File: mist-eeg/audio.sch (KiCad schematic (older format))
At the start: 30 parts, among them J3 Audio, U10 ADAU1372, Y1 12.288 MHz @ max 20 pF

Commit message: Hooked-up the SoM
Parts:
- removed Y1: 12.288 MHz @ max 20 pF, Crystal:Crystal_SMD_Abracon_ABM8G-4Pin_3.2x2.5mm, symbol Device:Crystal_GND24_Small
- renumbered TP9 to TP10, TP5 to TP6, TP6 to TP7, TP7 to TP8, TP8 to TP9
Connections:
- net labels added: MCLK
- net labels removed: XI, XO
- wire segments 143 -> 133
- no-connect marks 2 -> 3
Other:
- note added: "TODO: protection diodes"
- note removed: "Crystal Oscillator"
- moved on the sheet: D3, R55, R56, R57, TP10, U10A

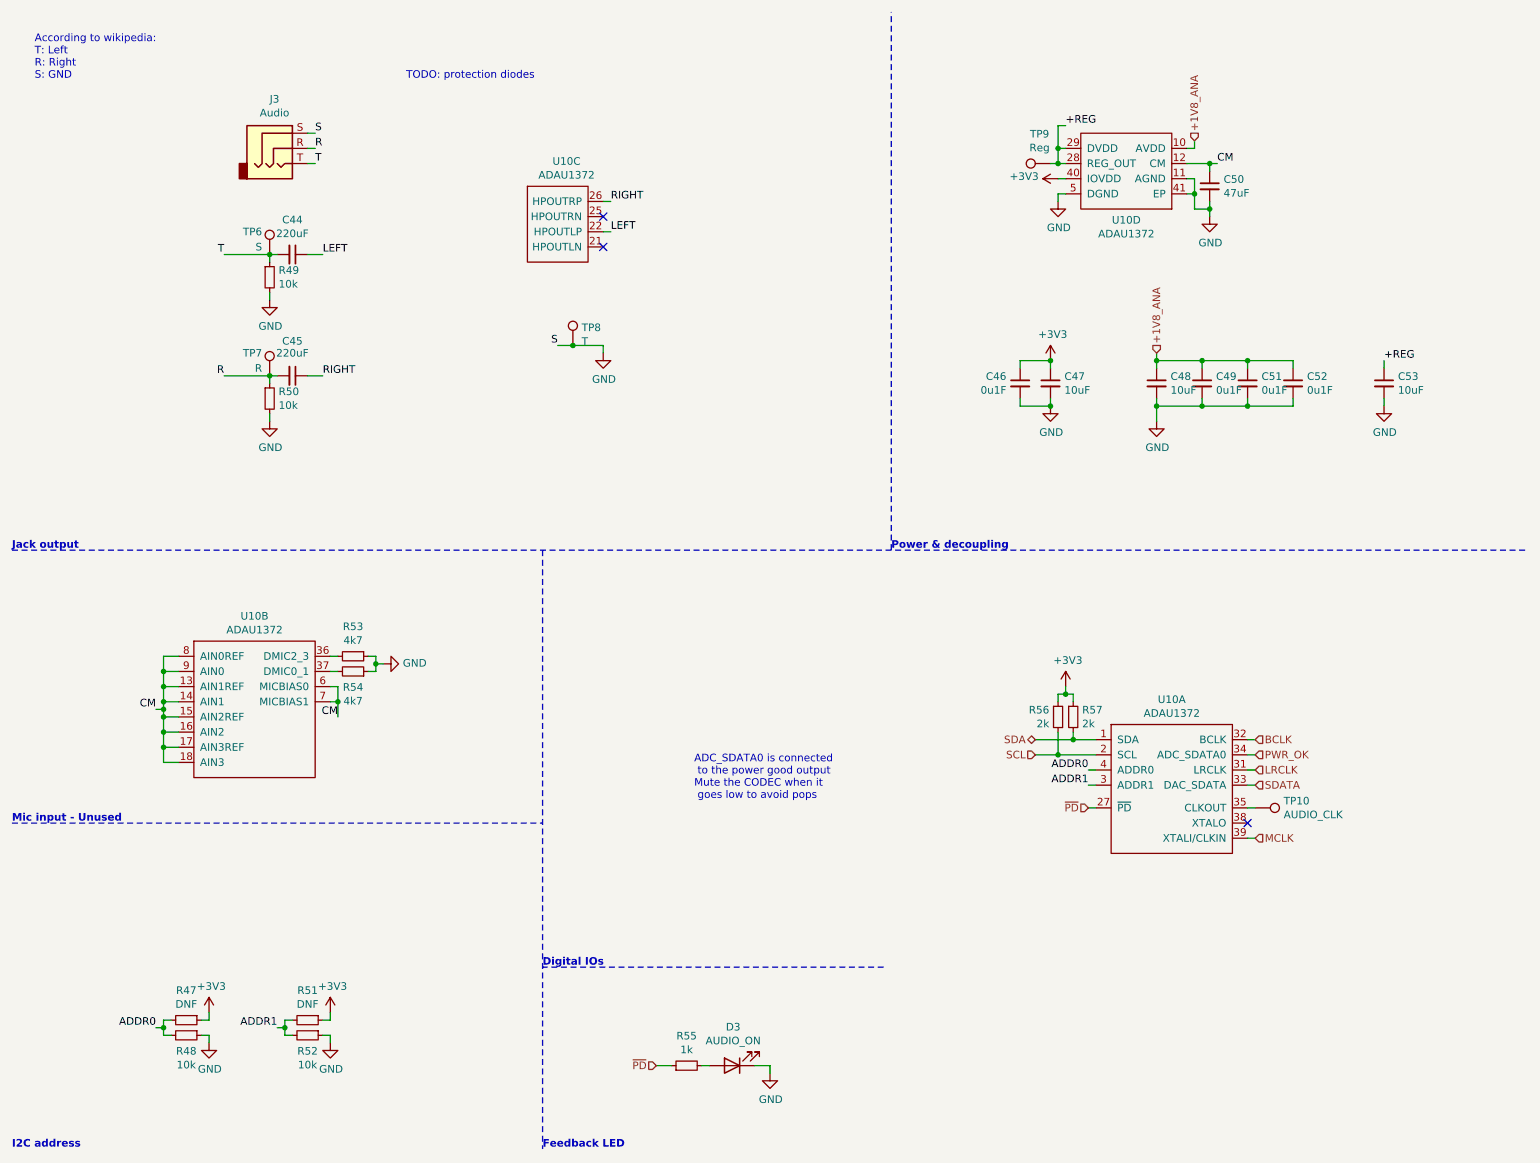
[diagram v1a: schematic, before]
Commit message: Finish schematic and create interface specifications
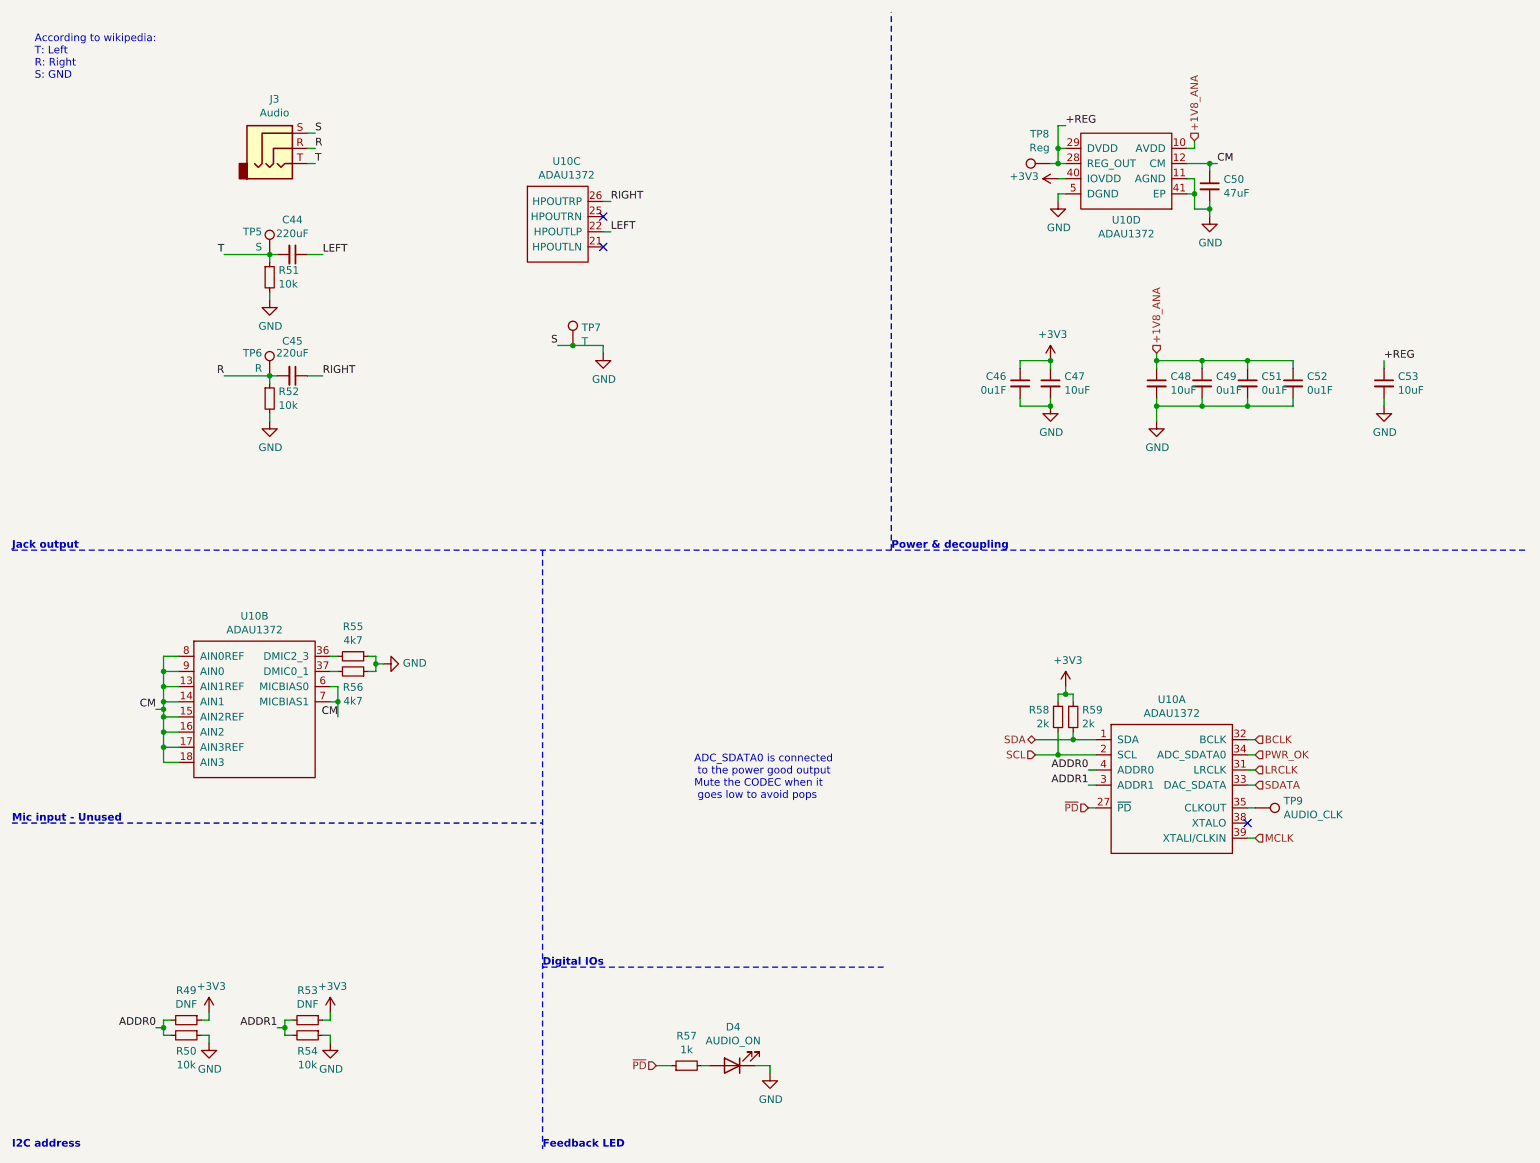
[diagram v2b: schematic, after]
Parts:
- renumbered D3 to D4, R47 to R49, R48 to R50, R49 to R51, R50 to R52, R51 to R53, R52 to R54, R53 to R55, R54 to R56, R55 to R57, R56 to R58, R57 to R59, TP6 to TP5, TP7 to TP6, TP8 to TP7, TP9 to TP8, TP10 to TP9
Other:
- note removed: "TODO: protection diodes"
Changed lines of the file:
@@
 $EndComp
 $Comp
-L Device:R_Small R49
+L Device:R_Small R51
 U 1 1 60ABF5BC
 P 2200 2250
-F 0 "R49" H 2259 2296 50  0000 L CNN
+F 0 "R51" H 2259 2296 50  0000 L CNN
 F 1 "10k" H 2259 2205 50  0000 L CNN
 F 2 "Resistor_SMD:R_0603_1608Metric" H 2200 2250 50  0001 C CNN
@@
 	2200 2400 2200 2350
 $Comp
-L Connector:TestPoint TP6
+L Connector:TestPoint TP5
 U 1 1 60AC1D50
 P 2200 2100
-F 0 "TP6" H 2150 2250 50  0000 R CNN
+F 0 "TP5" H 2150 2250 50  0000 R CNN
 F 1 "S" H 2150 2150 50  0000 R CNN
 F 2 "TestPoint:TestPoint_Pad_D1.0mm" H 2400 2100 50  0001 C CNN
@@
 $EndComp
 $Comp
-L Device:R_Small R50
+L Device:R_Small R52
 U 1 1 60AC80C7
 P 2200 3050
-F 0 "R50" H 2259 3096 50  0000 L CNN
+F 0 "R52" H 2259 3096 50  0000 L CNN
 F 1 "10k" H 2259 3005 50  0000 L CNN
 F 2 "Resistor_SMD:R_0603_1608Metric" H 2200 3050 50  0001 C CNN
@@
 	2200 3200 2200 3150
 $Comp
-L Connector:TestPoint TP8
+L Connector:TestPoint TP7
 U 1 1 60AC9A75
 P 4200 2700
-F 0 "TP8" H 4258 2818 50  0000 L CNN
+F 0 "TP7" H 4258 2818 50  0000 L CNN
 F 1 "T" H 4258 2727 50  0000 L CNN
 F 2 "TestPoint:TestPoint_Pad_D1.0mm" H 4400 2700 50  0001 C CNN
@@
 	1900 2900 2200 2900
 $Comp
-L Connector:TestPoint TP7
+L Connector:TestPoint TP6
 U 1 1 60AC80D7
 P 2200 2900
-F 0 "TP7" H 2150 3050 50  0000 R CNN
+F 0 "TP6" H 2150 3050 50  0000 R CNN
 F 1 "R" H 2150 2950 50  0000 R CNN
 F 2 "TestPoint:TestPoint_Pad_D1.0mm" H 2400 2900 50  0001 C CNN
@@
 	8300 1600 8300 1700
 $Comp
-L power:GND #PWR077
+L power:GND #PWR078
 U 1 1 60AE94E1
 P 7400 1750
-F 0 "#PWR077" H 7400 1500 50  0001 C CNN
+F 0 "#PWR078" H 7400 1500 50  0001 C CNN
 F 1 "GND" H 7405 1577 50  0000 C CNN
 F 2 "" H 7400 1750 50  0001 C CNN
@@
 	7450 1400 7400 1400
 $Comp
-L Connector:TestPoint TP9
+L Connector:TestPoint TP8
 U 1 1 60AF62E6
 P 7350 1500
-F 0 "TP9" V 7545 1572 50  0000 C CNN
+F 0 "TP8" V 7545 1572 50  0000 C CNN
 F 1 "Reg" V 7454 1572 50  0000 C CNN
 F 2 "TestPoint:TestPoint_Pad_D1.0mm" H 7550 1500 50  0001 C CNN
@@
 SCL
 $Comp
-L Device:R_Small R57
+L Device:R_Small R59
 U 1 1 60B0947B
 P 7500 5150
-F 0 "R57" H 7559 5196 50  0000 L CNN
+F 0 "R59" H 7559 5196 50  0000 L CNN
 F 1 "2k" H 7559 5105 50  0000 L CNN
 F 2 "Resistor_SMD:R_0201_0603Metric" H 7500 5150 50  0001 C CNN
@@
 	7500 5250 7500 5300
 $Comp
-L Device:R_Small R56
+L Device:R_Small R58
 U 1 1 60B0B8D0
 P 7400 5150
-F 0 "R56" H 7342 5196 50  0000 R CNN
+F 0 "R58" H 7342 5196 50  0000 R CNN
 F 1 "2k" H 7342 5105 50  0000 R CNN
 F 2 "Resistor_SMD:R_0201_0603Metric" H 7400 5150 50  0001 C CNN
@@
 ADDR0
 $Comp
-L Device:R_Small R47
+L Device:R_Small R49
 U 1 1 60B1A008
 P 1650 7150
-F 0 "R47" V 1454 7150 50  0000 C CNN
+F 0 "R49" V 1454 7150 50  0000 C CNN
 F 1 "DNF" V 1545 7150 50  0000 C CNN
 F 2 "Resistor_SMD:R_0603_1608Metric" H 1650 7150 50  0001 C CNN
@@
 	1800 7100 1800 7150
 $Comp
-L power:GND #PWR066
+L power:GND #PWR067
 U 1 1 60B1D99B
 P 1800 7300
-F 0 "#PWR066" H 1800 7050 50  0001 C CNN
+F 0 "#PWR067" H 1800 7050 50  0001 C CNN
 F 1 "GND" H 1805 7127 50  0000 C CNN
 F 2 "" H 1800 7300 50  0001 C CNN
@@
 ADDR1
 $Comp
-L Device:R_Small R51
+L Device:R_Small R53
 U 1 1 60B213C1
 P 2450 7150
-F 0 "R51" V 2254 7150 50  0000 C CNN
+F 0 "R53" V 2254 7150 50  0000 C CNN
 F 1 "DNF" V 2345 7150 50  0000 C CNN
 F 2 "Resistor_SMD:R_0603_1608Metric" H 2450 7150 50  0001 C CNN
@@
 	2600 7100 2600 7150
 $Comp
-L power:GND #PWR070
+L power:GND #PWR071
 U 1 1 60B213D6
 P 2600 7300
-F 0 "#PWR070" H 2600 7050 50  0001 C CNN
+F 0 "#PWR071" H 2600 7050 50  0001 C CNN
 F 1 "GND" H 2605 7127 50  0000 C CNN
 F 2 "" H 2600 7300 50  0001 C CNN
@@
 Power & decoupling
 $Comp
-L power:GND #PWR075
+L power:GND #PWR076
 U 1 1 60C1A59D
 P 7350 3100
-F 0 "#PWR075" H 7350 2850 50  0001 C CNN
+F 0 "#PWR076" H 7350 2850 50  0001 C CNN
 F 1 "GND" H 7355 2927 50  0000 C CNN
 F 2 "" H 7350 3100 50  0001 C CNN
@@
 	9550 2800 9550 2850
 $Comp
-L power:GND #PWR081
+L power:GND #PWR082
 U 1 1 60C65040
 P 9550 3100
-F 0 "#PWR081" H 9550 2850 50  0001 C CNN
+F 0 "#PWR082" H 9550 2850 50  0001 C CNN
 F 1 "GND" H 9555 2927 50  0000 C CNN
 F 2 "" H 9550 3100 50  0001 C CNN
@@
 	8700 5300 8650 5300
 $Comp
-L Connector:TestPoint TP10
+L Connector:TestPoint TP9
 U 1 1 60C89384
 P 8700 5750
-F 0 "TP10" V 8654 5938 50  0000 L CNN
+F 0 "TP9" V 8654 5938 50  0000 L CNN
 F 1 "AUDIO_CLK" V 8745 5938 50  0000 L CNN
 F 2 "TestPoint:TestPoint_Pad_D1.0mm" H 8900 5750 50  0001 C CNN
@@
 	8700 5750 8650 5750
 $Comp
-L Device:LED D3
+L Device:LED D4
 U 1 1 60CD54B6
 P 5250 7450
-F 0 "D3" H 5243 7195 50  0000 C CNN
+F 0 "D4" H 5243 7195 50  0000 C CNN
 F 1 "AUDIO_ON" H 5243 7286 50  0000 C CNN
 F 2 "LED_SMD:LED_0603_1608Metric" H 5250 7450 50  0001 C CNN
@@
 ~PD~
 $Comp
-L Device:R_Small R55
+L Device:R_Small R57
 U 1 1 60CD6214
 P 4950 7450
-F 0 "R55" V 5146 7450 50  0000 C CNN
+F 0 "R57" V 5146 7450 50  0000 C CNN
 F 1 "1k" V 5055 7450 50  0000 C CNN
 F 2 "Resistor_SMD:R_0402_1005Metric" H 4950 7450 50  0001 C CNN
@@
 	5050 7450 5100 7450
 $Comp
-L power:GND #PWR073
+L power:GND #PWR074
 U 1 1 60CDB6F6
 P 5500 7500
-F 0 "#PWR073" H 5500 7250 50  0001 C CNN
+F 0 "#PWR074" H 5500 7250 50  0001 C CNN
 F 1 "GND" H 5505 7327 50  0000 C CNN
 F 2 "" H 5500 7500 50  0001 C CNN
@@
 	4000 4050 4000 8000
 $Comp
-L Device:R_Small R48
+L Device:R_Small R50
 U 1 1 60B1A002
 P 1650 7250
-F 0 "R48" V 1754 7250 50  0000 C CNN
+F 0 "R50" V 1754 7250 50  0000 C CNN
 F 1 "10k" V 1845 7250 50  0000 C CNN
 F 2 "Resistor_SMD:R_0603_1608Metric" H 1650 7250 50  0001 C CNN
@@
 $EndComp
 $Comp
-L Device:R_Small R52
+L Device:R_Small R54
 U 1 1 60FB0630
 P 2450 7250
-F 0 "R52" V 2554 7250 50  0000 C CNN
+F 0 "R54" V 2554 7250 50  0000 C CNN
 F 1 "10k" V 2645 7250 50  0000 C CNN
 F 2 "Resistor_SMD:R_0603_1608Metric" H 2450 7250 50  0001 C CNN
@@
 	7400 1600 7450 1600
 $Comp
-L power:GND #PWR080
+L power:GND #PWR081
 U 1 1 611D8E7E
 P 8400 1850
-F 0 "#PWR080" H 8400 1600 50  0001 C CNN
+F 0 "#PWR081" H 8400 1600 50  0001 C CNN
 F 1 "GND" H 8405 1677 50  0000 C CNN
 F 2 "" H 8400 1850 50  0001 C CNN
@@
 $EndComp
 $Comp
-L power:GND #PWR079
+L power:GND #PWR080
 U 1 1 611D9111
 P 8050 3200
-F 0 "#PWR079" H 8050 2950 50  0001 C CNN
+F 0 "#PWR080" H 8050 2950 50  0001 C CNN
 F 1 "GND" H 8055 3027 50  0000 C CNN
 F 2 "" H 8050 3200 50  0001 C CNN
@@
 $EndComp
 $Comp
-L power:GND #PWR072
+L power:GND #PWR073
 U 1 1 611D94F5
 P 4400 2750
-F 0 "#PWR072" H 4400 2500 50  0001 C CNN
+F 0 "#PWR073" H 4400 2500 50  0001 C CNN
 F 1 "GND" H 4405 2577 50  0000 C CNN
 F 2 "" H 4400 2750 50  0001 C CNN
@@
 $EndComp
 $Comp
-L power:GND #PWR067
+L power:GND #PWR068
 U 1 1 611DC98D
 P 2200 2400
-F 0 "#PWR067" H 2200 2150 50  0001 C CNN
+F 0 "#PWR068" H 2200 2150 50  0001 C CNN
 F 1 "GND" H 2205 2227 50  0000 C CNN
 F 2 "" H 2200 2400 50  0001 C CNN
@@
 $EndComp
 $Comp
-L power:GND #PWR068
+L power:GND #PWR069
 U 1 1 611DCDAF
 P 2200 3200
-F 0 "#PWR068" H 2200 2950 50  0001 C CNN
+F 0 "#PWR069" H 2200 2950 50  0001 C CNN
 F 1 "GND" H 2205 3027 50  0000 C CNN
 F 2 "" H 2200 3200 50  0001 C CNN
@@
 	2650 4750 2600 4750
 $Comp
-L power:GND #PWR071
+L power:GND #PWR072
 U 1 1 60B73760
 P 2950 4800
-F 0 "#PWR071" H 2950 4550 50  0001 C CNN
+F 0 "#PWR072" H 2950 4550 50  0001 C CNN
 F 1 "GND" V 2955 4672 50  0000 R CNN
 F 2 "" H 2950 4800 50  0001 C CNN
@@
 	2900 4800 2950 4800
 $Comp
-L Device:R_Small R54
+L Device:R_Small R56
 U 1 1 60B6399F
 P 2750 4850
-F 0 "R54" V 2646 4850 50  0000 C CNN
+F 0 "R56" V 2646 4850 50  0000 C CNN
 F 1 "4k7" V 2555 4850 50  0000 C CNN
 F 2 "Resistor_SMD:R_0201_0603Metric" H 2750 4850 50  0001 C CNN
@@
 $EndComp
 $Comp
-L Device:R_Small R53
+L Device:R_Small R55
 U 1 1 60B60CF8
 P 2750 4750
-F 0 "R53" V 2554 4750 50  0000 C CNN
+F 0 "R55" V 2554 4750 50  0000 C CNN
 F 1 "4k7" V 2645 4750 50  0000 C CNN
 F 2 "Resistor_SMD:R_0201_0603Metric" H 2750 4750 50  0001 C CNN
@@
 	7350 1500 7400 1500
 $Comp
-L power:+3V3 #PWR074
+L power:+3V3 #PWR075
 U 1 1 61142B16
 P 7350 2800
-F 0 "#PWR074" H 7350 2650 50  0001 C CNN
+F 0 "#PWR075" H 7350 2650 50  0001 C CNN
 F 1 "+3V3" H 7365 2973 50  0000 C CNN
 F 2 "" H 7350 2800 50  0001 C CNN
@@
 $EndComp
 $Comp
-L power:+3V3 #PWR078
+L power:+3V3 #PWR079
 U 1 1 611790DA
 P 7450 4950
-F 0 "#PWR078" H 7450 4800 50  0001 C CNN
+F 0 "#PWR079" H 7450 4800 50  0001 C CNN
 F 1 "+3V3" H 7465 5123 50  0000 C CNN
 F 2 "" H 7450 4950 50  0001 C CNN
@@
 $EndComp
 $Comp
-L power:+3V3 #PWR076
+L power:+3V3 #PWR077
 U 1 1 611B1AA0
 P 7400 1600
-F 0 "#PWR076" H 7400 1450 50  0001 C CNN
+F 0 "#PWR077" H 7400 1450 50  0001 C CNN
 F 1 "+3V3" V 7415 1728 50  0000 L CNN
 F 2 "" H 7400 1600 50  0001 C CNN
@@
 Connection ~ 7350 3100
 $Comp
-L power:+3V3 #PWR065
+L power:+3V3 #PWR066
 U 1 1 611C292F
 P 1800 7100
-F 0 "#PWR065" H 1800 6950 50  0001 C CNN
+F 0 "#PWR066" H 1800 6950 50  0001 C CNN
 F 1 "+3V3" H 1815 7273 50  0000 C CNN
 F 2 "" H 1800 7100 50  0001 C CNN
@@
 $EndComp
 $Comp
-L power:+3V3 #PWR069
+L power:+3V3 #PWR070
 U 1 1 611C2E6E
 P 2600 7100
-F 0 "#PWR069" H 2600 6950 50  0001 C CNN
+F 0 "#PWR070" H 2600 6950 50  0001 C CNN
 F 1 "+3V3" H 2615 7273 50  0000 C CNN
 F 2 "" H 2600 7100 50  0001 C CNN
@@
 Text HLabel 8700 5950 2    50   Input ~ 0
 MCLK
-Text Notes 3100 950  0    50   ~ 0
-TODO: protection diodes
 $EndSCHEMATC

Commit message: Update footprints based upon piece availability & generate manufacturing files
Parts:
- C44, C45, C50: footprint Capacitor_SMD:C_1206_3216Metric -> Capacitor_SMD:C_1210_3225Metric
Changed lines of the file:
@@
 F 0 "C44" V 2121 2100 50  0000 C CNN
 F 1 "220uF" V 2212 2100 50  0000 C CNN
-F 2 "Capacitor_SMD:C_1206_3216Metric" H 2350 2100 50  0001 C CNN
+F 2 "Capacitor_SMD:C_1210_3225Metric" H 2350 2100 50  0001 C CNN
 F 3 "~" H 2350 2100 50  0001 C CNN
 	1    2350 2100
@@
 F 0 "C45" V 2121 2900 50  0000 C CNN
 F 1 "220uF" V 2200 2900 50  0000 C CNN
-F 2 "Capacitor_SMD:C_1206_3216Metric" H 2350 2900 50  0001 C CNN
+F 2 "Capacitor_SMD:C_1210_3225Metric" H 2350 2900 50  0001 C CNN
 F 3 "~" H 2350 2900 50  0001 C CNN
 	1    2350 2900
@@
 F 0 "C50" H 8492 1696 50  0000 L CNN
 F 1 "47uF" H 8492 1605 50  0000 L CNN
-F 2 "Capacitor_SMD:C_1206_3216Metric" H 8400 1650 50  0001 C CNN
+F 2 "Capacitor_SMD:C_1210_3225Metric" H 8400 1650 50  0001 C CNN
 F 3 "~" H 8400 1650 50  0001 C CNN
 	1    8400 1650
